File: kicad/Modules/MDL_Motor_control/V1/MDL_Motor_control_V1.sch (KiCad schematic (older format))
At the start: 9 parts, among them M1 DC_Motor, Q1 Q2N2222, U1 TopTour

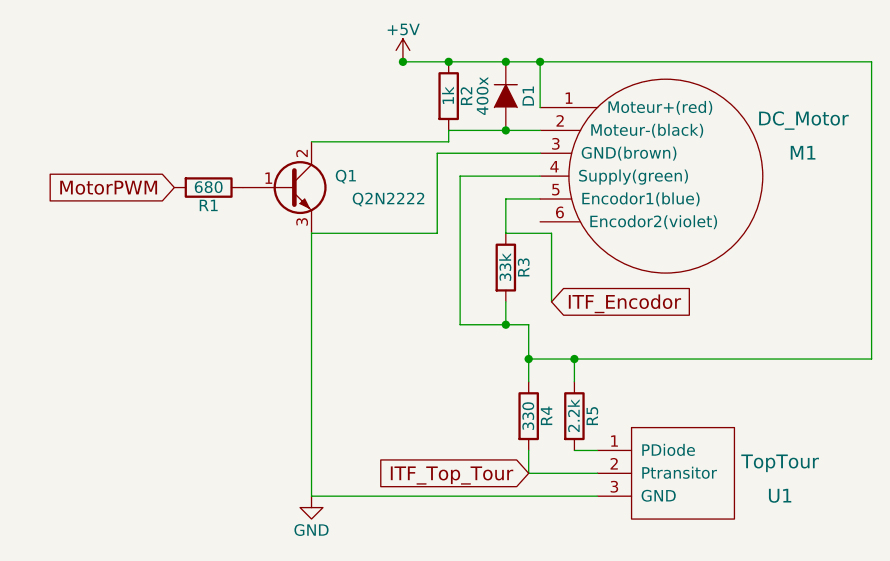
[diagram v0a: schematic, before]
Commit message: update DB_HV, update librairy and librairy path for MDL
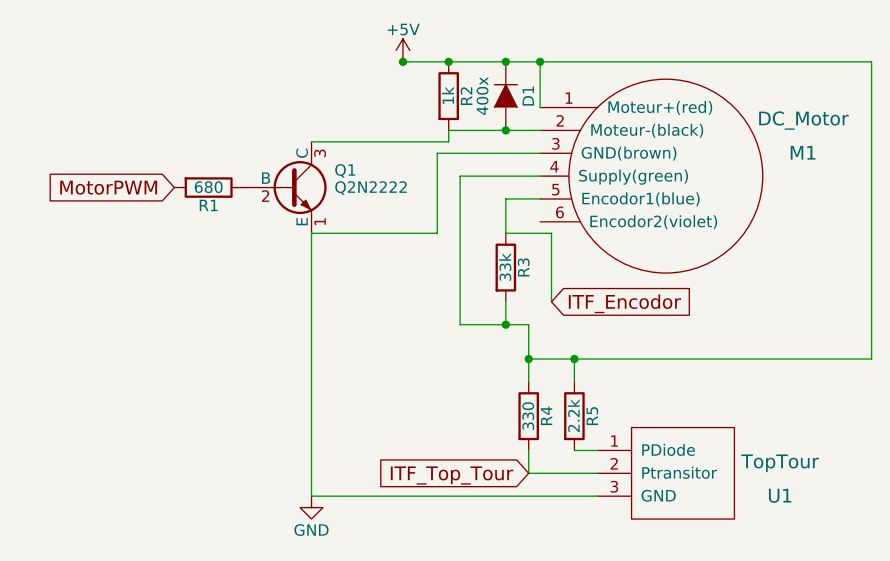
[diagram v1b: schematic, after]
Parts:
- removed Q1: Q2N2222, symbol Q_NPN_BCE
- added Q1: Q2N2222, symbol Q2N2222
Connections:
- net GND: now also Q1.1 (E)
- net at D1.2 (A), M1.2 (Moteur-(black)), R2.2: now also Q1.3 (C)
- net at R1.1: now also Q1.2 (B)
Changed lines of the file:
@@
 LIBS:valves
 LIBS:echopen
+LIBS:MDL_Motor_control_V1-cache
 EELAYER 25 0
 EELAYER END
@@
 	0    1    1    0
 $EndComp
-$Comp
-L Q_NPN_BCE Q1
-U 1 1 57A4E84F
-P 4500 2550
-F 0 "Q1" H 4800 2600 50  0000 R CNN
-F 1 "Q2N2222" H 5100 2500 50  0000 R CNN
-F 2 "" H 4700 2650 50  0000 C CNN
-F 3 "" H 4500 2550 50  0000 C CNN
-	1    4500 2550
-	1    0    0    -1
-$EndComp
 Text GLabel 4000 2550 0    60   Input ~ 0
 MotorPWM
@@
 	1    0    0    -1
 $EndComp
+$Comp
+L Q2N2222 Q1
+U 1 1 57B42CCD
+P 4500 2550
+F 0 "Q1" H 4700 2625 50  0000 L CNN
+F 1 "Q2N2222" H 4700 2550 50  0000 L CNN
+F 2 "" H 4700 2475 50  0000 L CIN
+F 3 "" H 4500 2550 50  0000 L CNN
+	1    4500 2550
+	1    0    0    -1
+$EndComp

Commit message: update MDLs with new librairy
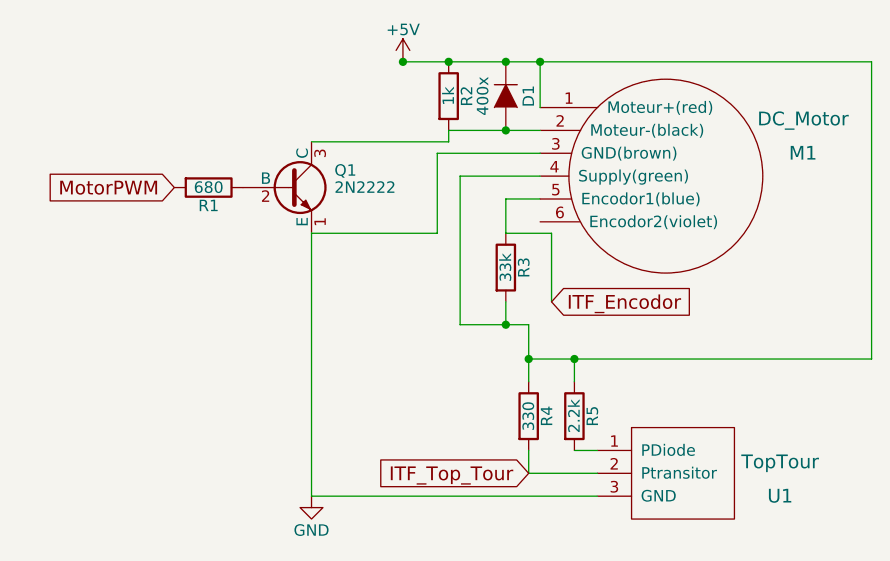
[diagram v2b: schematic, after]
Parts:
- removed Q1: Q2N2222, symbol Q2N2222
- added Q1: 2N2222, symbol 2N2222
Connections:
- net GND: now also Q1.1 (E)
- net at D1.2 (A), M1.2 (Moteur-(black)), R2.2: now also Q1.3 (C)
- net at R1.1: now also Q1.2 (B)
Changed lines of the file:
@@
 $EndComp
 $Comp
-L Q2N2222 Q1
-U 1 1 57B42CCD
+L 2N2222 Q1
+U 1 1 57B46E8E
 P 4500 2550
 F 0 "Q1" H 4700 2625 50  0000 L CNN
-F 1 "Q2N2222" H 4700 2550 50  0000 L CNN
+F 1 "2N2222" H 4700 2550 50  0000 L CNN
 F 2 "" H 4700 2475 50  0000 L CIN
 F 3 "" H 4500 2550 50  0000 L CNN
